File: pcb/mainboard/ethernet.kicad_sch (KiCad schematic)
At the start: 20 parts, among them J1001 8P8C_LED_Shielded, U1001 USBLC6-4SC6 / AZC199-04S

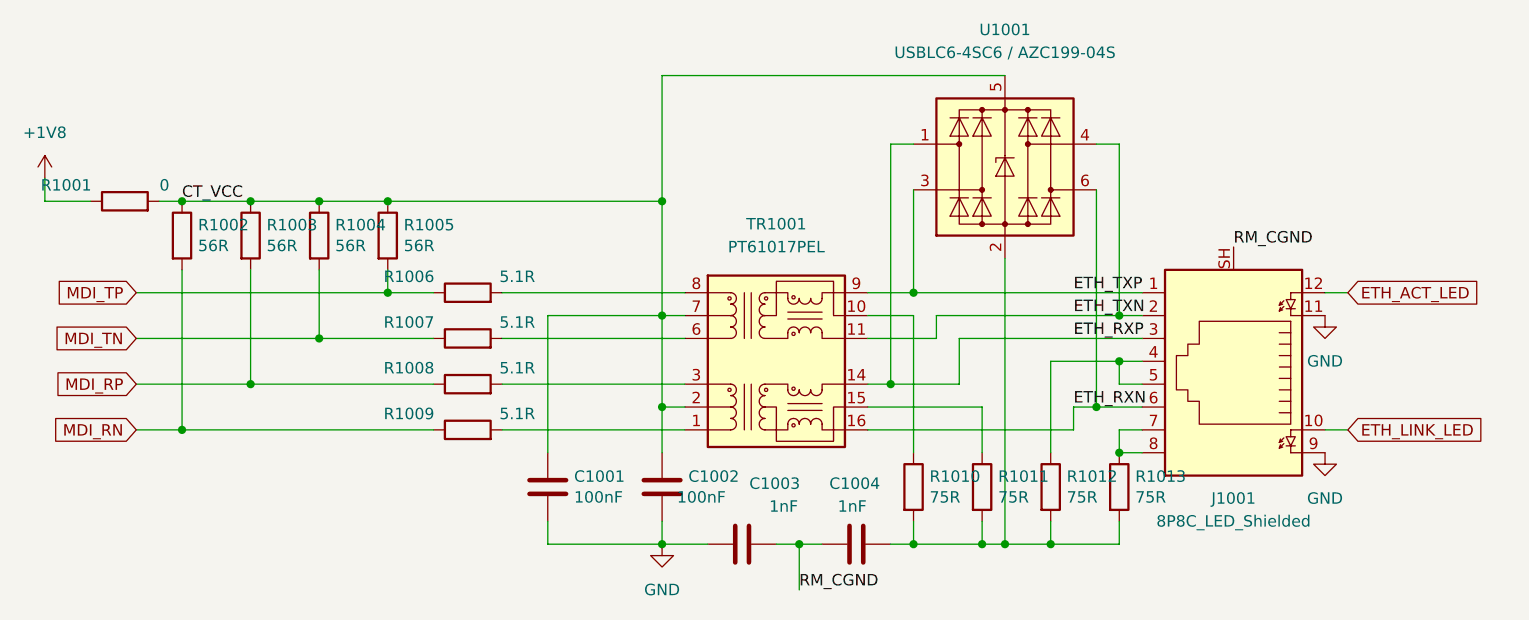
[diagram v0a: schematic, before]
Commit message: pcb: initial placement for mb
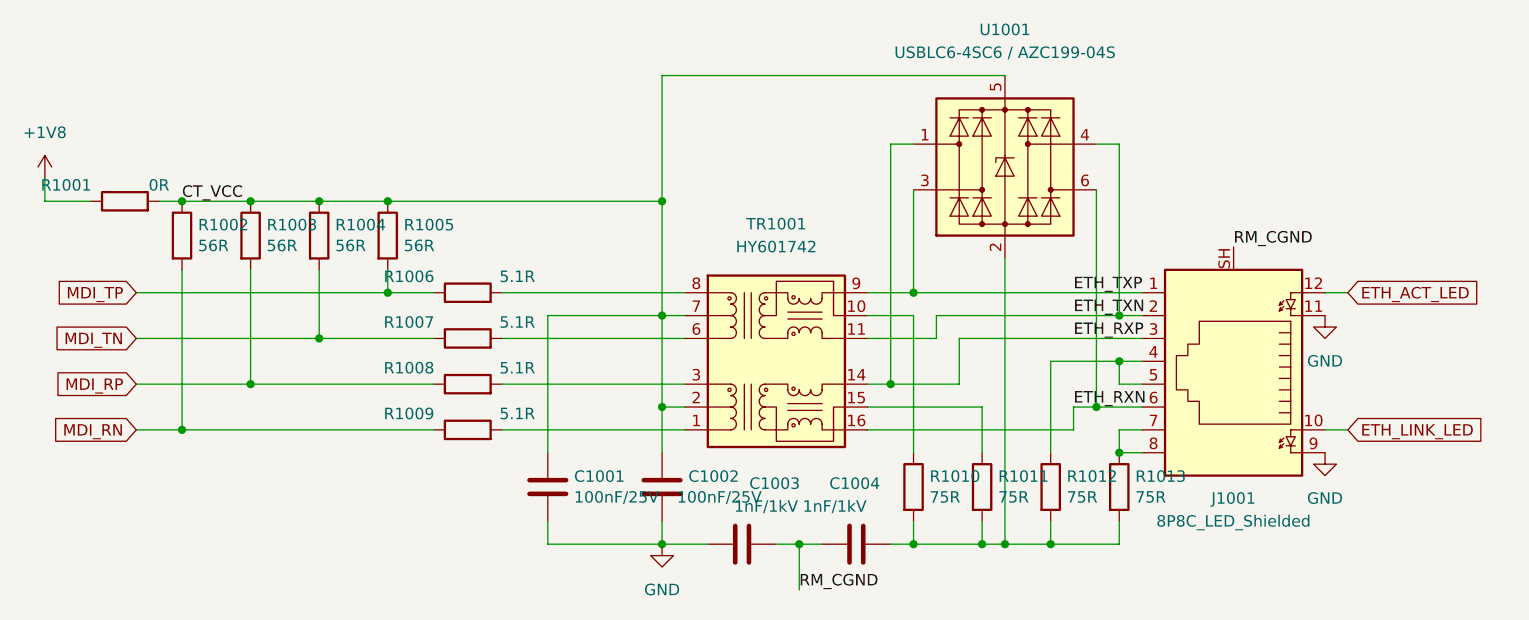
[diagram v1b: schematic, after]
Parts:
- C1001, C1002: value 100nF -> 100nF/25V; LCSC (none) -> C56392; Ref.Price (none) -> 0.0023
- C1003, C1004: value 1nF -> 1nF/1kV; footprint Capacitor_SMD:C_0402_1005Metric -> Capacitor_SMD:C_1206_3216Metric; LCSC (none) -> C2687445; Ref.Price (none) -> 0.0162
- J1001: LCSC (none) -> C2828084; Ref.Price (none) -> 0.4074
- R1001: value 0 -> 0R; LCSC (none) -> C60485; Ref.Price (none) -> 0.0008
- R1002, R1003, R1004, R1005: LCSC (none) -> C137857; Ref.Price (none) -> 0.0007
- R1006, R1007, R1008, R1009: LCSC (none) -> C137853; Ref.Price (none) -> 0.0012
- R1010, R1011, R1012, R1013: LCSC (none) -> C137841; Ref.Price (none) -> 0.0016
- TR1001: value PT61017PEL -> HY601742; LCSC (none) -> C55684; Ref.Price (none) -> 0.8151
- U1001: LCSC (none) -> C558419; Ref.Price (none) -> 0.06
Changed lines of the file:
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@@
       (effects (font (size 1.27 1.27)) (justify left))
     )
-    (property "Value" "0" (id 1) (at 87.503 76.962 90)
+    (property "Value" "0R" (id 1) (at 87.503 76.962 90)
       (effects (font (size 1.27 1.27)) (justify left))
     )
@@
       (effects (font (size 1.27 1.27)) hide)
     )
+    (property "LCSC" "C60485" (id 4) (at 82.55 78.74 0)
+      (effects (font (size 1.27 1.27)) hide)
+    )
+    (property "Ref.Price" "0.0008" (id 5) (at 82.55 78.74 0)
+      (effects (font (size 1.27 1.27)) hide)
+    )
     (pin "1")
     (pin "2")
@@
       (effects (font (size 1.27 1.27)) hide)
     )
+    (property "LCSC" "C137857" (id 4) (at 88.9 82.55 0)
+      (effects (font (size 1.27 1.27)) hide)
+    )
+    (property "Ref.Price" "0.0007" (id 5) (at 88.9 82.55 0)
+      (effects (font (size 1.27 1.27)) hide)
+    )
     (pin "1")
     (pin "2")
@@
       (effects (font (size 1.27 1.27)) hide)
     )
+    (property "LCSC" "C137857" (id 4) (at 96.52 82.55 0)
+      (effects (font (size 1.27 1.27)) hide)
+    )
+    (property "Ref.Price" "0.0007" (id 5) (at 96.52 82.55 0)
+      (effects (font (size 1.27 1.27)) hide)
+    )
     (pin "1")
     (pin "2")
@@
       (effects (font (size 1.27 1.27)) hide)
     )
+    (property "LCSC" "C137857" (id 4) (at 104.14 82.55 0)
+      (effects (font (size 1.27 1.27)) hide)
+    )
+    (property "Ref.Price" "0.0007" (id 5) (at 104.14 82.55 0)
+      (effects (font (size 1.27 1.27)) hide)
+    )
     (pin "1")
     (pin "2")
@@
       (effects (font (size 1.27 1.27)) hide)
     )
+    (property "LCSC" "C137857" (id 4) (at 111.76 82.55 0)
+      (effects (font (size 1.27 1.27)) hide)
+    )
+    (property "Ref.Price" "0.0007" (id 5) (at 111.76 82.55 0)
+      (effects (font (size 1.27 1.27)) hide)
+    )
     (pin "1")
     (pin "2")
@@
       (effects (font (size 1.27 1.27)) hide)
     )
+    (property "LCSC" "C137853" (id 4) (at 120.65 88.9 0)
+      (effects (font (size 1.27 1.27)) hide)
+    )
+    (property "Ref.Price" "0.0012" (id 5) (at 120.65 88.9 0)
+      (effects (font (size 1.27 1.27)) hide)
+    )
     (pin "1")
     (pin "2")
@@
       (effects (font (size 1.27 1.27)) hide)
     )
+    (property "LCSC" "C137853" (id 4) (at 120.65 93.98 0)
+      (effects (font (size 1.27 1.27)) hide)
+    )
+    (property "Ref.Price" "0.0012" (id 5) (at 120.65 93.98 0)
+      (effects (font (size 1.27 1.27)) hide)
+    )
     (pin "1")
     (pin "2")
@@
       (effects (font (size 1.27 1.27)) hide)
     )
+    (property "LCSC" "C137853" (id 4) (at 120.65 99.06 0)
+      (effects (font (size 1.27 1.27)) hide)
+    )
+    (property "Ref.Price" "0.0012" (id 5) (at 120.65 99.06 0)
+      (effects (font (size 1.27 1.27)) hide)
+    )
     (pin "1")
     (pin "2")
@@
       (effects (font (size 1.27 1.27)) hide)
     )
+    (property "LCSC" "C137853" (id 4) (at 120.65 104.14 0)
+      (effects (font (size 1.27 1.27)) hide)
+    )
+    (property "Ref.Price" "0.0012" (id 5) (at 120.65 104.14 0)
+      (effects (font (size 1.27 1.27)) hide)
+    )
     (pin "1")
     (pin "2")
@@
       (effects (font (size 1.27 1.27)) hide)
     )
+    (property "LCSC" "C137841" (id 4) (at 170.18 110.49 0)
+      (effects (font (size 1.27 1.27)) hide)
+    )
+    (property "Ref.Price" "0.0016" (id 5) (at 170.18 110.49 0)
+      (effects (font (size 1.27 1.27)) hide)
+    )
     (pin "1")
     (pin "2")
@@
       (effects (font (size 1.27 1.27)) hide)
     )
+    (property "LCSC" "C137841" (id 4) (at 177.8 110.49 0)
+      (effects (font (size 1.27 1.27)) hide)
+    )
+    (property "Ref.Price" "0.0016" (id 5) (at 177.8 110.49 0)
+      (effects (font (size 1.27 1.27)) hide)
+    )
     (pin "1")
     (pin "2")
@@
       (effects (font (size 1.27 1.27)) hide)
     )
+    (property "LCSC" "C137841" (id 4) (at 185.42 110.49 0)
+      (effects (font (size 1.27 1.27)) hide)
+    )
+    (property "Ref.Price" "0.0016" (id 5) (at 185.42 110.49 0)
+      (effects (font (size 1.27 1.27)) hide)
+    )
     (pin "1")
     (pin "2")
@@
       (effects (font (size 1.27 1.27)) hide)
     )
+    (property "LCSC" "C137841" (id 4) (at 193.04 110.49 0)
+      (effects (font (size 1.27 1.27)) hide)
+    )
+    (property "Ref.Price" "0.0016" (id 5) (at 193.04 110.49 0)
+      (effects (font (size 1.27 1.27)) hide)
+    )
     (pin "1")
     (pin "2")
@@
       (effects (font (size 1.27 1.27)) (justify left))
     )
-    (property "Value" "100nF" (id 1) (at 132.461 111.633 0)
+    (property "Value" "100nF/25V" (id 1) (at 132.461 111.633 0)
       (effects (font (size 1.27 1.27)) (justify left))
     )
@@
       (effects (font (size 1.27 1.27)) hide)
     )
+    (property "LCSC" "C56392" (id 4) (at 129.54 110.49 0)
+      (effects (font (size 1.27 1.27)) hide)
+    )
+    (property "Ref.Price" "0.0023" (id 5) (at 129.54 110.49 0)
+      (effects (font (size 1.27 1.27)) hide)
+    )
     (pin "1")
     (pin "2")
@@
       (effects (font (size 1.27 1.27)) (justify left))
     )
-    (property "Value" "100nF" (id 1) (at 143.891 111.633 0)
+    (property "Value" "100nF/25V" (id 1) (at 143.891 111.633 0)
       (effects (font (size 1.27 1.27)) (justify left))
     )
@@
       (effects (font (size 1.27 1.27)) hide)
     )
+    (property "LCSC" "C56392" (id 4) (at 142.24 110.49 0)
+      (effects (font (size 1.27 1.27)) hide)
+    )
+    (property "Ref.Price" "0.0023" (id 5) (at 142.24 110.49 0)
+      (effects (font (size 1.27 1.27)) hide)
+    )
     (pin "1")
     (pin "2")
@@
       (effects (font (size 1.27 1.27)) (justify left))
     )
-    (property "Value" "1nF" (id 1) (at 157.353 112.649 90)
-      (effects (font (size 1.27 1.27)) (justify left))
-    )
-    (property "Footprint" "Capacitor_SMD:C_0402_1005Metric" (id 2) (at 154.94 115.8748 0)
+    (property "Value" "1nF/1kV" (id 1) (at 157.353 112.649 90)
+      (effects (font (size 1.27 1.27)) (justify left))
+    )
+    (property "Footprint" "Capacitor_SMD:C_1206_3216Metric" (id 2) (at 154.94 115.8748 0)
       (effects (font (size 1.27 1.27)) hide)
     )
@@
       (effects (font (size 1.27 1.27)) hide)
     )
+    (property "LCSC" "C2687445" (id 4) (at 151.13 116.84 0)
+      (effects (font (size 1.27 1.27)) hide)
+    )
+    (property "Ref.Price" "0.0162" (id 5) (at 151.13 116.84 0)
+      (effects (font (size 1.27 1.27)) hide)
+    )
     (pin "1")
     (pin "2")
@@
       (effects (font (size 1.27 1.27)) (justify left))
     )
-    (property "Value" "1nF" (id 1) (at 164.973 112.649 90)
-      (effects (font (size 1.27 1.27)) (justify left))
-    )
-    (property "Footprint" "Capacitor_SMD:C_0402_1005Metric" (id 2) (at 167.64 115.8748 0)
+    (property "Value" "1nF/1kV" (id 1) (at 164.973 112.649 90)
+      (effects (font (size 1.27 1.27)) (justify left))
+    )
+    (property "Footprint" "Capacitor_SMD:C_1206_3216Metric" (id 2) (at 167.64 115.8748 0)
       (effects (font (size 1.27 1.27)) hide)
     )
     (property "Datasheet" "~" (id 3) (at 163.83 116.84 0)
+      (effects (font (size 1.27 1.27)) hide)
+    )
+    (property "LCSC" "C2687445" (id 4) (at 163.83 116.84 0)
+      (effects (font (size 1.27 1.27)) hide)
+    )
+    (property "Ref.Price" "0.0162" (id 5) (at 163.83 116.84 0)
       (effects (font (size 1.27 1.27)) hide)
     )
@@
     (in_bom yes) (on_board yes) (fields_autoplaced)
     (property "Reference" "TR1001" (id 0) (at 154.94 81.28 0))
-    (property "Value" "PT61017PEL" (id 1) (at 154.94 83.82 0))
+    (property "Value" "HY601742" (id 1) (at 154.94 83.82 0))
     (property "Footprint" "Transformer_SMD:Transformer_Ethernet_Bourns_PT61017PEL" (id 2) (at 154.94 109.22 0)
       (effects (font (size 1.27 1.27)) hide)
     )
     (property "Datasheet" "https://www.bourns.com/docs/Product-Datasheets/PT61017PEL.pdf" (id 3) (at 137.16 87.63 0)
+      (effects (font (size 1.27 1.27)) hide)
+    )
+    (property "LCSC" "C55684" (id 4) (at 154.94 96.52 0)
+      (effects (font (size 1.27 1.27)) hide)
+    )
+    (property "Ref.Price" "0.8151" (id 5) (at 154.94 96.52 0)
       (effects (font (size 1.27 1.27)) hide)
     )
@@
       (effects (font (size 1.27 1.27)) hide)
     )
+    (property "LCSC" "C558419" (id 4) (at 180.34 74.93 0)
+      (effects (font (size 1.27 1.27)) hide)
+    )
+    (property "Ref.Price" "0.06" (id 5) (at 180.34 74.93 0)
+      (effects (font (size 1.27 1.27)) hide)
+    )
     (pin "1")
     (pin "2")
@@
       (effects (font (size 1.27 1.27)) hide)
     )
+    (property "LCSC" "C2828084" (id 4) (at 205.74 96.52 0)
+      (effects (font (size 1.27 1.27)) hide)
+    )
+    (property "Ref.Price" "0.4074" (id 5) (at 205.74 96.52 0)
+      (effects (font (size 1.27 1.27)) hide)
+    )

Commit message: pcb: r0.1 mb routing done
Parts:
- added C1005: 100nF/25V, Capacitor_SMD:C_0402_1005Metric, symbol Device:C
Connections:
- net CT_VCC: now also C1005.1
- net GND: now also C1005.2
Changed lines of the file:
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@@
   (junction (at 170.18 116.84) (diameter 0) (color 0 0 0 0))
   (junction (at 177.8 116.84) (diameter 0) (color 0 0 0 0))
+  (junction (at 180.34 64.77) (diameter 0) (color 0 0 0 0))
   (junction (at 180.34 116.84) (diameter 0) (color 0 0 0 0))
   (junction (at 185.42 116.84) (diameter 0) (color 0 0 0 0))
@@
     (stroke (width 0) (type default) (color 0 0 0 0))
   )
+  (wire (pts (xy 180.34 64.77) (xy 195.58 64.77))
+    (stroke (width 0) (type default) (color 0 0 0 0))
+  )
   (wire (pts (xy 180.34 85.09) (xy 180.34 116.84))
     (stroke (width 0) (type default) (color 0 0 0 0))
@@
     (pin "1")
   )
+  (symbol (lib_id "power:GND") (at 195.58 72.39 0) (unit 1)
+    (in_bom yes) (on_board yes) (fields_autoplaced)
+    (property "Reference" "#PWR0122" (id 0) (at 195.58 78.74 0)
+      (effects (font (size 1.27 1.27)) hide)
+    )
+    (property "Value" "GND" (id 1) (at 195.58 77.47 0))
+    (property "Footprint" "" (id 2) (at 195.58 72.39 0)
+      (effects (font (size 1.27 1.27)) hide)
+    )
+    (property "Datasheet" "" (id 3) (at 195.58 72.39 0)
+      (effects (font (size 1.27 1.27)) hide)
+    )
+    (pin "1")
+  )
   (symbol (lib_id "power:GND") (at 215.9 91.44 0) (unit 1)
     (in_bom yes) (on_board yes) (fields_autoplaced)
@@
       (effects (font (size 1.27 1.27)) hide)
     )
+    (pin "1")
+    (pin "2")
+  )
+  (symbol (lib_id "Device:C") (at 195.58 68.58 0) (unit 1)
+    (in_bom yes) (on_board yes)
+    (property "Reference" "C1005" (id 0) (at 198.501 67.4116 0)
+      (effects (font (size 1.27 1.27)) (justify left))
+    )
+    (property "Value" "100nF/25V" (id 1) (at 197.231 69.723 0)
+      (effects (font (size 1.27 1.27)) (justify left))
+    )
+    (property "Footprint" "Capacitor_SMD:C_0402_1005Metric" (id 2) (at 196.5452 72.39 0)
+      (effects (font (size 1.27 1.27)) hide)
+    )
+    (property "Datasheet" "~" (id 3) (at 195.58 68.58 0)
+      (effects (font (size 1.27 1.27)) hide)
+    )
+    (property "LCSC" "C56392" (id 4) (at 195.58 68.58 0)
+      (effects (font (size 1.27 1.27)) hide)
+    )
+    (property "Ref.Price" "0.0023" (id 5) (at 195.58 68.58 0)
+      (effects (font (size 1.27 1.27)) hide)
+    )
